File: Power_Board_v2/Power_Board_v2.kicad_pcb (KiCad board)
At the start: 2 copper layers, 33 parts, among them J1 Conn_02x16_Odd_Even, Q1 MMBT5551L, U2 HUSB237-AA001-DN06R, U3 BQ24074RGT, U4 INA219AxDCN SOT-23

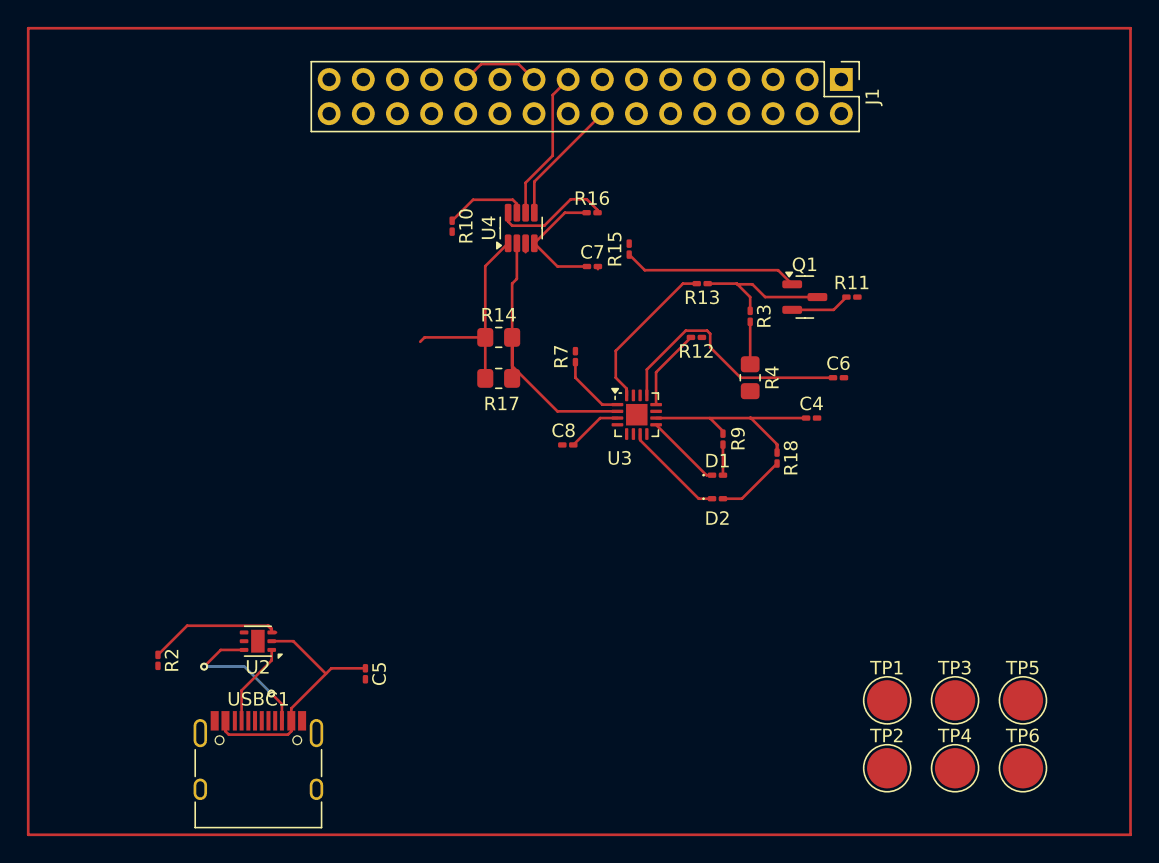
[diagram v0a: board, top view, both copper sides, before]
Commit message: Updated footprints and battery label
I HATE THE IMPERIAL SYSTEM
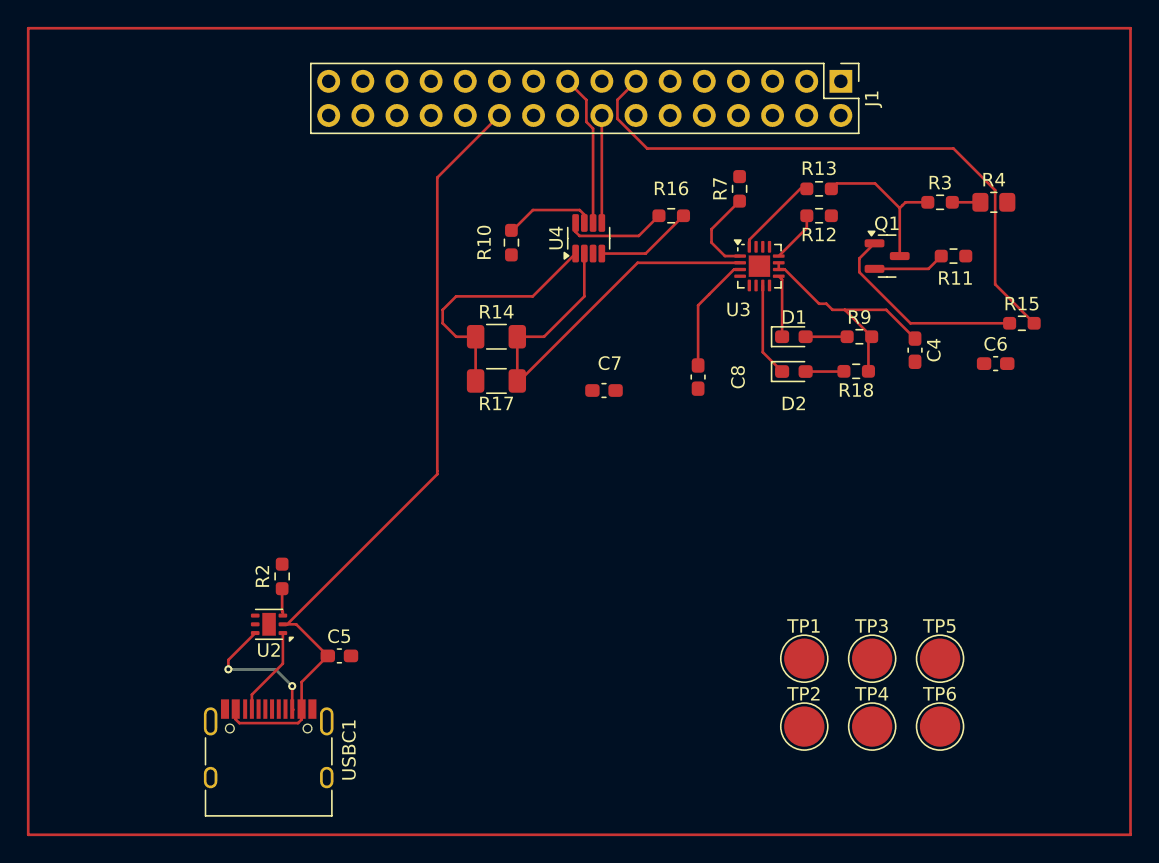
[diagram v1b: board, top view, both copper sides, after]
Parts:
- C4, C5, C6, C7, C8: footprint Capacitor_SMD:C_0201_0603Metric_Pad0.64x0.40mm_HandSolder -> Capacitor_SMD:C_0603_1608Metric_Pad1.08x0.95mm_HandSolder
- D1, D2: footprint LED_SMD:LED_0201_0603Metric_Pad0.64x0.40mm_HandSolder -> LED_SMD:LED_0603_1608Metric_Pad1.05x0.95mm_HandSolder
- R10, R11, R12, R13, R15, R16, R18, R2, R3, R7, R9: footprint Resistor_SMD:R_0201_0603Metric_Pad0.64x0.40mm_HandSolder -> Resistor_SMD:R_0603_1608Metric_Pad0.98x0.95mm_HandSolder
- R14, R17: footprint Resistor_SMD:R_0805_2012Metric_Pad1.20x1.40mm_HandSolder -> Resistor_SMD:R_1206_3216Metric_Pad1.30x1.75mm_HandSolder
- moved R15 29.7 mm to (262.1, 125.0), turned to 0 degrees
- moved R4 22.3 mm to (260.0, 116.0), turned to 0 degrees
- moved R7 17.5 mm to (241.1, 115.0)
- moved R3 16.5 mm to (256.0, 116.0), turned to 0 degrees
- moved U3 14.3 mm to (242.6, 120.8)
- moved R12 12.9 mm to (247.0, 117.0)
- moved R9 12.7 mm to (250.0, 126.0), turned to 180 degrees
- moved D1 11.8 mm to (245.1, 126.0)
- moved C6 11.7 mm to (260.1, 128.0)
- moved R13 11.2 mm to (247.0, 115.0)
- moved R2 11.1 mm to (207.1, 143.8), turned to 90 degrees
- moved D2 11.0 mm to (245.1, 128.6)
- moved C8 10.9 mm to (238.0, 129.0), turned to 90 degrees
- moved C7 9.27 mm to (231.0, 130.0)
- moved C4 9.20 mm to (254.1, 127.0), turned to -90 degrees
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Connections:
- net /BATT renamed /Battery
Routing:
- net /FAST_CHARGE_CTRL: track 0.00 -> 44.8 mm
- net /High Voltage (9V): track 38.4 -> 60.5 mm
- net /Battery: track 41.9 -> 60.4 mm
- net Net-(U2-VSET): track 10.7 -> 2.02 mm
- net GND: track 7.03 -> 0.00 mm
- net Net-(U3-ISET): track 11.7 -> 6.37 mm
- net Net-(Q1-B): track 13.0 -> 15.4 mm
- net Net-(D2-A): track 5.11 -> 2.85 mm
- net /5V Out: track 9.46 -> 7.24 mm
- net Net-(U3-ILIM): track 6.07 -> 3.86 mm
- net /LOAD: track 16.6 -> 18.3 mm
- net /I2C1_SCL: track 9.46 -> 8.00 mm
- net Net-(U3-TS): track 5.11 -> 6.49 mm
- net Net-(U4-A1): track 8.78 -> 7.61 mm
- net Net-(D1-K): track 5.71 -> 4.60 mm
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
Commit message: Same as previous
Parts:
- J1: value Conn_02x16_Odd_Even -> PH2.54-01-16PZS
- U4: value INA219AxDCN SOT-23 -> INA219AIDCNR
- USBC1: value ~ -> TYPE-C-31-M-12
- moved TP1 4.14 mm to (241.9, 151.0)
- moved TP2 4.14 mm to (241.9, 156.1)
- moved TP3 4.14 mm to (246.9, 151.0)
- moved TP4 4.14 mm to (246.9, 156.1)
- moved TP5 4.14 mm to (252.0, 151.0)
- moved TP6 4.14 mm to (252.0, 156.1)
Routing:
- net /High Voltage (9V): track 60.5 -> 61.8 mm

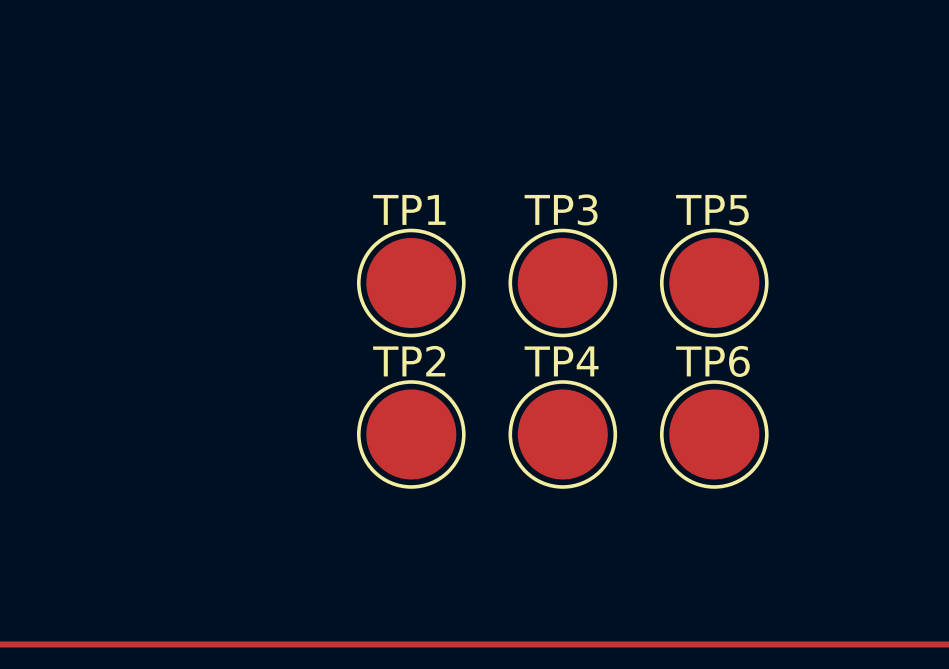
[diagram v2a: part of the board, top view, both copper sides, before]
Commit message: Updated some stuffs
Tried to add the battery connector, but it wouldn't work
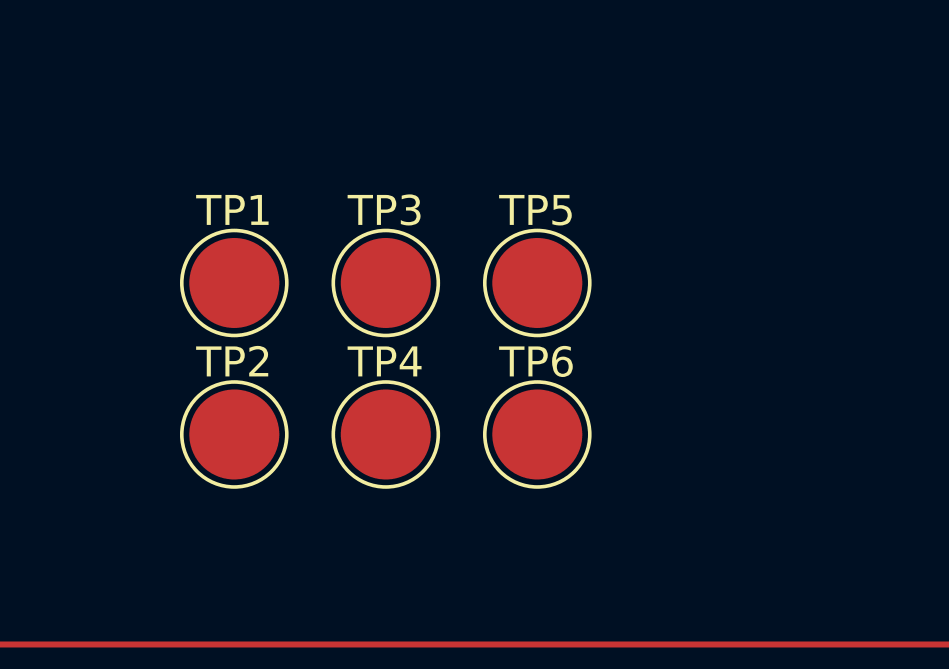
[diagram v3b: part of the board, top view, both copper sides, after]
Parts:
- moved TP1 5.90 mm to (236.0, 151.0)
- moved TP2 5.90 mm to (236.0, 156.1)
- moved TP5 5.90 mm to (246.1, 151.0)
- moved TP6 5.90 mm to (246.1, 156.1)
- moved TP3 5.90 mm to (241.1, 151.0)
- moved TP4 5.90 mm to (241.1, 156.1)
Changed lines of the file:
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@@
 	)
 	(paper "A4")
+	(title_block
+		(title "PCB Design for Power Board of MM")
+		(date "2025-03-28")
+		(rev "3")
+		(comment 1 "Author: Joshua Smith (SMTJOS022)")
+		(comment 2 "Author: Ebrahim Bhyat (HYEBR002)")
+	)
 	(layers
 		(0 "F.Cu" signal)
@@
 	(footprint "TestPoint:TestPoint_Pad_D3.0mm"
 		(layer "F.Cu")
-		(at 252 156.05)
+		(at 246.1 156.05)
 		(descr "SMD pad as test Point, diameter 3.0mm")
 		(tags "test point SMD pad")
@@
 	(footprint "TestPoint:TestPoint_Pad_D3.0mm"
 		(layer "F.Cu")
-		(at 252 151)
+		(at 246.1 151)
 		(descr "SMD pad as test Point, diameter 3.0mm")
 		(tags "test point SMD pad")
@@
 	(footprint "TestPoint:TestPoint_Pad_D3.0mm"
 		(layer "F.Cu")
-		(at 241.9 156.05)
+		(at 236 156.05)
 		(descr "SMD pad as test Point, diameter 3.0mm")
 		(tags "test point SMD pad")
@@
 	(footprint "TestPoint:TestPoint_Pad_D3.0mm"
 		(layer "F.Cu")
-		(at 246.95 151)
+		(at 241.05 151)
 		(descr "SMD pad as test Point, diameter 3.0mm")
 		(tags "test point SMD pad")
@@
 	(footprint "TestPoint:TestPoint_Pad_D3.0mm"
 		(layer "F.Cu")
-		(at 246.95 156.05)
+		(at 241.05 156.05)
 		(descr "SMD pad as test Point, diameter 3.0mm")
 		(tags "test point SMD pad")
@@
 	(footprint "TestPoint:TestPoint_Pad_D3.0mm"
 		(layer "F.Cu")
-		(at 241.9 151)
+		(at 236 151)
 		(descr "SMD pad as test Point, diameter 3.0mm")
 		(tags "test point SMD pad")

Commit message: Minor tweaks
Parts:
- added J2: Conn_01x02, Connector_JST:JST_PH_S2B-PH-K_1x02_P2.00mm_Horizontal, F.Cu at (262.0, 157.0)
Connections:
- C6 pad 2: GND -> Net-(U3-EN1)
- TP6 pad 1: GND -> Net-(U3-EN1)
- U3 pad 14: GND -> Net-(U3-EN1)
- U3 pad 4: GND -> Net-(U3-EN1)
- U3 pad 5: GND -> /LOAD
- U3 pad 6: GND -> Net-(U3-EN1)
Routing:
- net /Battery: track 60.4 -> 162.3 mm
- net /5V Out: track 7.24 -> 40.0 mm
- net /LOAD: track 18.3 -> 33.5 mm
